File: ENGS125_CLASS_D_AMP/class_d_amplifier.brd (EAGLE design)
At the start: 100 x 80 mm, 24 parts, among them J1 BANANA_JACK_CT3151, J2 BANANA_JACK_CT3151, J3 BANANA_JACK_CT3151, J4 BANANA_JACK_CT3151, J5 BANANA_JACK_CT3151, J6 BANANA_JACK_CT3151, M1 BSC050NE2LSATMA1, M2 BSC050NE2LSATMA1, U1 LTC6992TSOT-23, U2 LTC4449

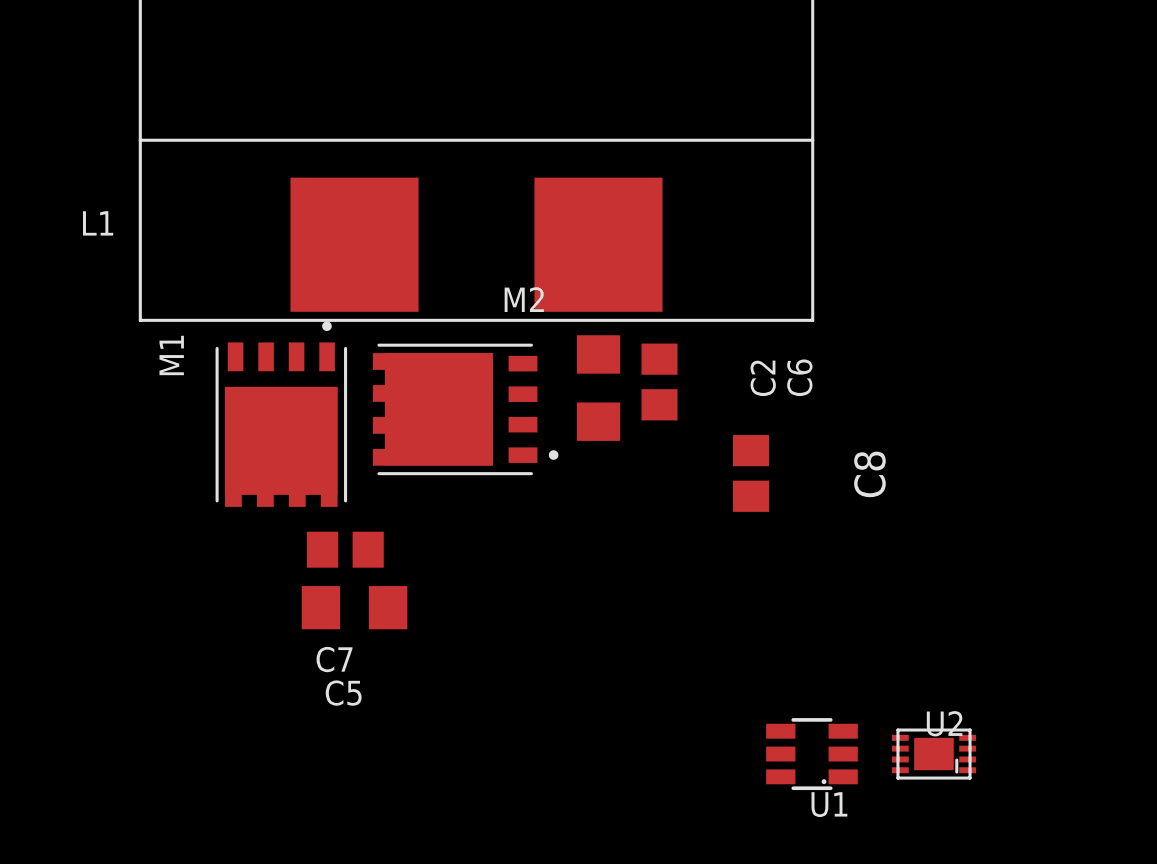
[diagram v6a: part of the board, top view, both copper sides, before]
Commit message: Generatedtop layer power polygons and placed vias
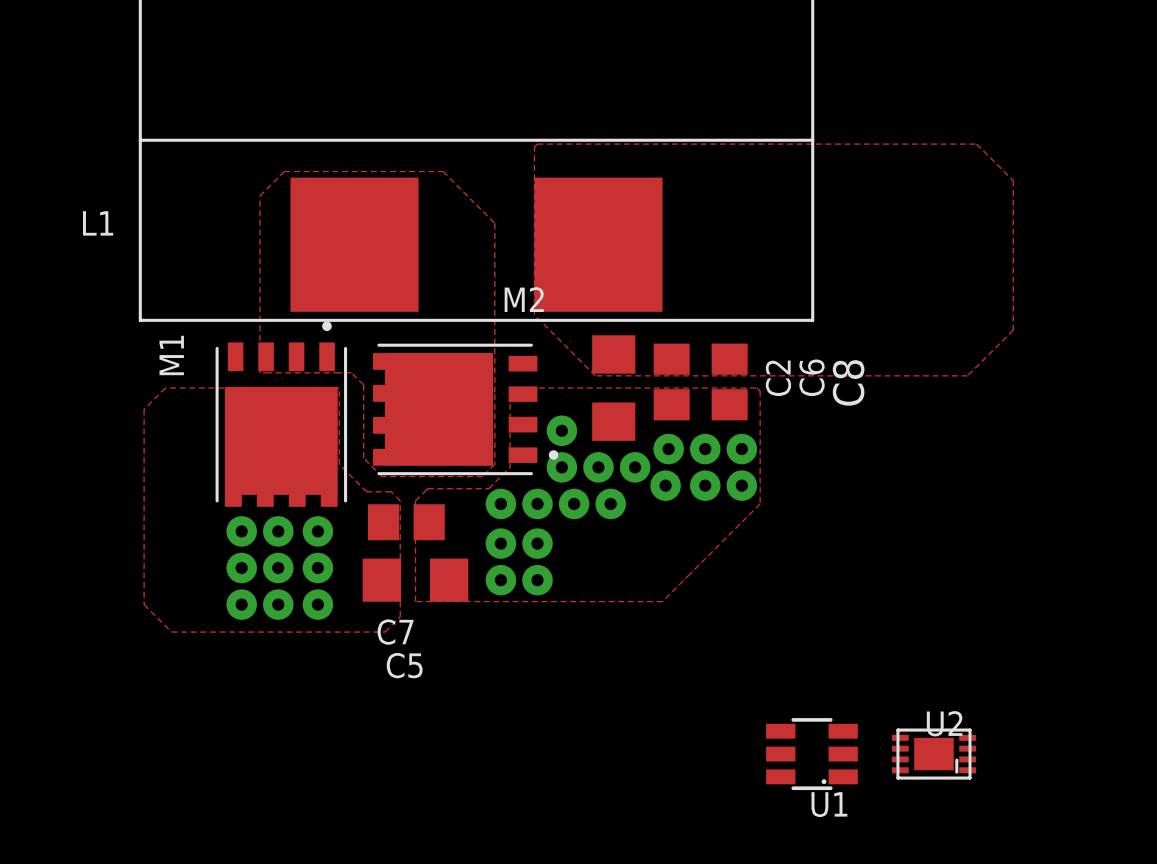
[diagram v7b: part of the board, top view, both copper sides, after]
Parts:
- moved C8 3.91 mm to (58.8, 30.7)
- moved C5 2.79 mm to (45.7, 22.5)
- moved C7 2.79 mm to (45.3, 24.9)
- moved C2 0.63 mm to (54.0, 30.5)
- moved C6 0.51 mm to (56.4, 30.7)
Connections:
- net VIN: now also M1.6, M1.7
- net VSW: now also M2.6, M2.7
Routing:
- added copper zone on layer 1, net GND
- added copper zone on layer 1, net VIN
- added copper zone on layer 1, net VOUT
- added copper zone on layer 1, net VSW

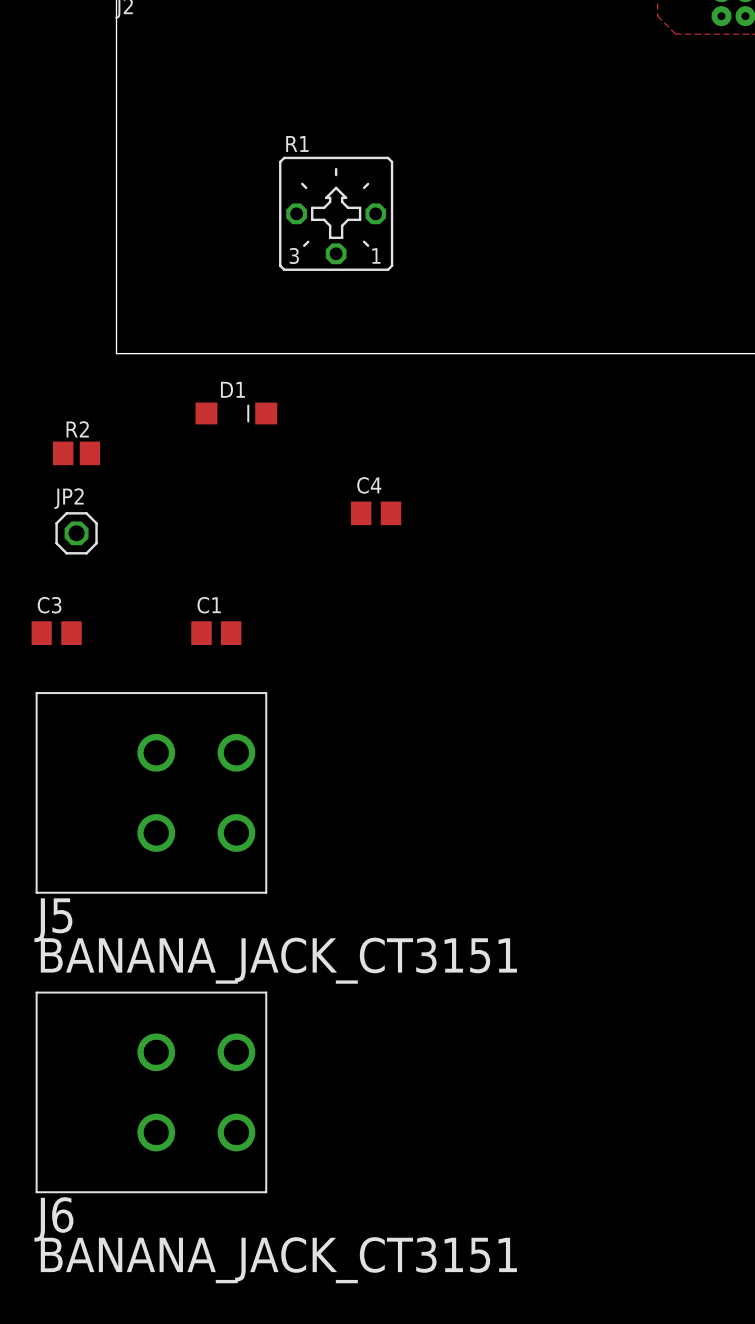
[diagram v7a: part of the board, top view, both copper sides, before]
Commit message: Removed component values from silkscreen
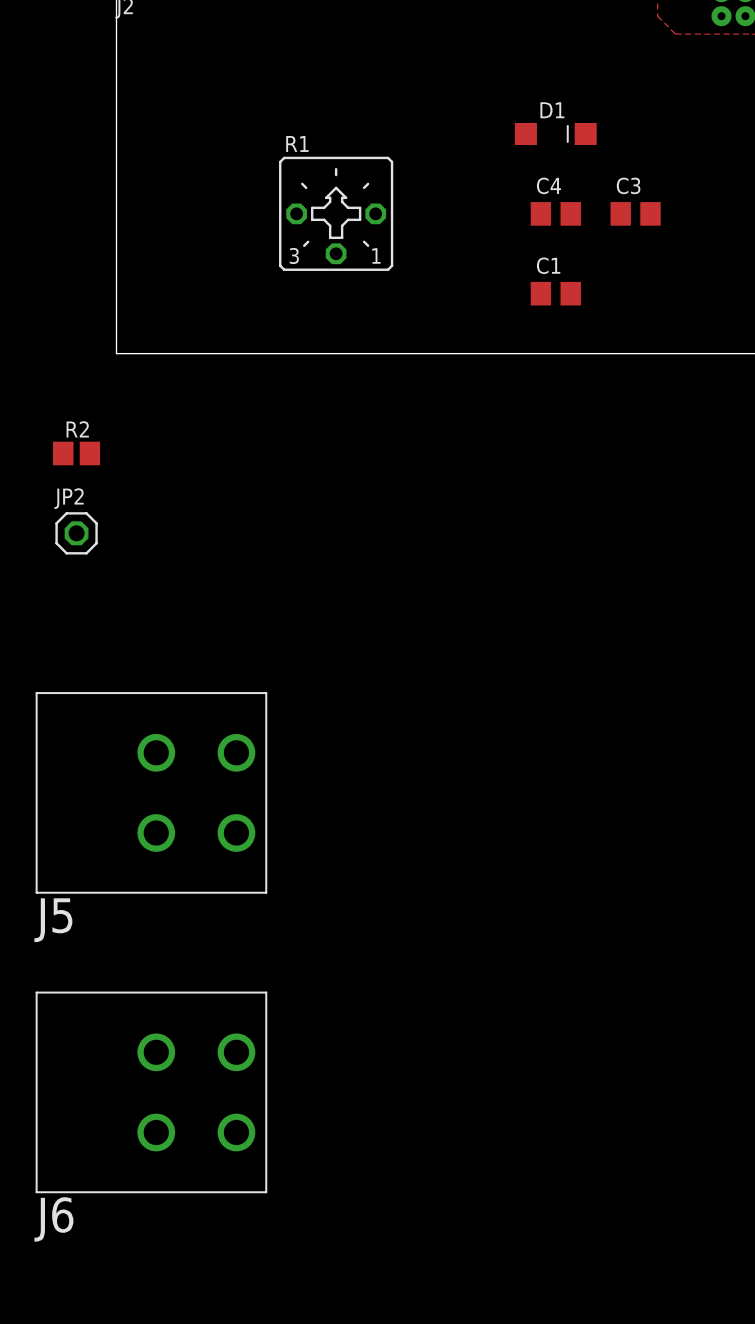
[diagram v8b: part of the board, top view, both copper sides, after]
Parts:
- moved C3 45.5 mm to (33.0, 8.89)
- moved C1 30.5 mm to (27.9, 3.81)
- moved D1 27.0 mm to (27.9, 14.0)
- moved C4 22.2 mm to (27.9, 8.89)
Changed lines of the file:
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@@
 </autorouter>
 <elements>
-<element name="C1" library="Engs125_library" package="C0805" value="0.1uF" x="6.35" y="-17.78" smashed="yes">
-<attribute name="NAME" x="5.08" y="-16.51" size="1.016" layer="25" font="fixed"/>
-<attribute name="VALUE" x="5.08" y="-20.32" size="1.016" layer="27" font="fixed"/>
+<element name="C1" library="Engs125_library" package="C0805" value="0.1uF" x="27.94" y="3.81" smashed="yes">
+<attribute name="NAME" x="26.67" y="5.08" size="1.016" layer="25" font="fixed"/>
 </element>
 <element name="C2" library="rcl" library_urn="urn:adsk.eagle:library:334" package="C1206" package3d_urn="urn:adsk.eagle:package:23618/2" value="1.5u" x="53.975" y="30.48" smashed="yes" rot="R270">
@@
 <attribute name="SPICEPREFIX" value="C" x="22.225" y="-15.24" size="1.778" layer="27" rot="R270" display="off"/>
 </element>
-<element name="C3" library="Engs125_library" package="C0805" value="1uF" x="-3.81" y="-17.78" smashed="yes">
-<attribute name="NAME" x="-5.08" y="-16.51" size="1.016" layer="25" font="fixed"/>
-<attribute name="VALUE" x="-5.08" y="-20.32" size="1.016" layer="27" font="fixed"/>
-</element>
-<element name="C4" library="Engs125_library" package="C0805" value="1uF" x="16.51" y="-10.16" smashed="yes">
-<attribute name="NAME" x="15.24" y="-8.89" size="1.016" layer="25" font="fixed"/>
-<attribute name="VALUE" x="15.24" y="-12.7" size="1.016" layer="27" font="fixed"/>
+<element name="C3" library="Engs125_library" package="C0805" value="1uF" x="33.02" y="8.89" smashed="yes">
+<attribute name="NAME" x="31.75" y="10.16" size="1.016" layer="25" font="fixed"/>
+</element>
+<element name="C4" library="Engs125_library" package="C0805" value="1uF" x="27.94" y="8.89" smashed="yes">
+<attribute name="NAME" x="26.67" y="10.16" size="1.016" layer="25" font="fixed"/>
 </element>
 <element name="C5" library="rcl" library_urn="urn:adsk.eagle:library:334" package="C1206" package3d_urn="urn:adsk.eagle:package:23618/2" value="4.7uF" x="45.72" y="22.479" smashed="yes">
@@
 <attribute name="NAME" x="44.069" y="19.812" size="1.016" layer="25" font="fixed"/>
 </element>
-<element name="D1" library="Engs125_library" package="SOD123" value="1N5819" x="7.62" y="-3.81" smashed="yes">
-<attribute name="NAME" x="6.52" y="-2.81" size="1.016" layer="25" font="fixed"/>
-<attribute name="VALUE" x="6.52" y="-6.11" size="1.016" layer="27" font="fixed"/>
+<element name="D1" library="Engs125_library" package="SOD123" value="1N5819" x="27.94" y="13.97" smashed="yes">
+<attribute name="NAME" x="26.84" y="14.97" size="1.016" layer="25" font="fixed"/>
 </element>
 <element name="L1" library="Engs125_library" package="SER2900" value="33u" x="48.26" y="50.8" smashed="yes">
@@
 <element name="J5" library="Engs125_lib_UPDATEFeb22" package="CT3151SP2_PCB_MOUNT" value="BANANA_JACK_CT3151" x="5.08" y="-27.94" smashed="yes">
 <attribute name="NAME" x="-5.08" y="-36.83" size="2.1844" layer="25" font="vector"/>
-<attribute name="VALUE" x="-5.08" y="-39.37" size="2.1844" layer="25" font="vector"/>
 </element>
 <element name="J6" library="Engs125_lib_UPDATEFeb22" package="CT3151SP2_PCB_MOUNT" value="BANANA_JACK_CT3151" x="5.08" y="-46.99" smashed="yes">
 <attribute name="NAME" x="-5.08" y="-55.88" size="2.1844" layer="25" font="vector"/>
-<attribute name="VALUE" x="-5.08" y="-58.42" size="2.1844" layer="25" font="vector"/>
 </element>
 <element name="C8" library="Engs125_library" package="C0805" value="0.1u" x="58.801" y="30.734" smashed="yes" rot="R270">
@@
 <wire x1="49.53" y1="5.08" x2="60.93" y2="16.19" width="0" layer="19" extent="1-1"/>
 <wire x1="46.99" y1="5.08" x2="49.53" y2="5.08" width="0" layer="19" extent="1-1"/>
-<wire x1="17.46" y1="-10.16" x2="46.99" y2="5.08" width="0" layer="19" extent="1-1"/>
-<wire x1="11.4554" y1="8.89" x2="17.46" y2="-10.16" width="0" layer="19" extent="1-1"/>
+<wire x1="28.89" y1="8.89" x2="46.99" y2="5.08" width="0" layer="19" extent="1-1"/>
+<wire x1="11.4554" y1="8.89" x2="28.89" y2="8.89" width="0" layer="19" extent="1-1"/>
 <wire x1="12.71" y1="27.93" x2="11.4554" y2="8.89" width="0" layer="19" extent="1-1"/>
 <wire x1="12.71" y1="33.03" x2="12.71" y2="27.93" width="0" layer="19" extent="1-1"/>
 <wire x1="7.61" y1="33.03" x2="12.71" y2="33.03" width="0" layer="19" extent="1-1"/>
 <wire x1="7.61" y1="27.93" x2="12.71" y2="27.93" width="0" layer="19" extent="1-1"/>
-<wire x1="-3.39" y1="-6.35" x2="17.46" y2="-10.16" width="0" layer="19" extent="1-1"/>
-<wire x1="-2.86" y1="-17.78" x2="-3.39" y2="-6.35" width="0" layer="19" extent="1-1"/>
-<wire x1="2.53" y1="-44.44" x2="-2.86" y2="-17.78" width="0" layer="19" extent="1-1"/>
+<wire x1="-3.39" y1="-6.35" x2="28.89" y2="8.89" width="0" layer="19" extent="1-1"/>
+<wire x1="33.97" y1="8.89" x2="-3.39" y2="-6.35" width="0" layer="19" extent="1-1"/>
+<wire x1="2.53" y1="-44.44" x2="33.97" y2="8.89" width="0" layer="19" extent="1-1"/>
 <wire x1="2.53" y1="-49.54" x2="2.53" y2="-44.44" width="0" layer="19" extent="1-1"/>
 <wire x1="7.63" y1="-49.54" x2="2.53" y2="-49.54" width="0" layer="19" extent="1-1"/>
@@
 <wire x1="65.91" y1="15.015" x2="65.91" y2="15.465" width="0" layer="19" extent="1-1"/>
 <wire x1="60.93" y1="15.24" x2="65.91" y2="15.465" width="0" layer="19" extent="1-1"/>
-<wire x1="15.56" y1="-10.16" x2="60.93" y2="15.24" width="0" layer="19" extent="1-1"/>
-<wire x1="5.72" y1="-3.81" x2="15.56" y2="-10.16" width="0" layer="19" extent="1-1"/>
-<wire x1="-4.76" y1="-17.78" x2="5.72" y2="-3.81" width="0" layer="19" extent="1-1"/>
-<wire x1="7.61" y1="43.17" x2="5.72" y2="-3.81" width="0" layer="19" extent="1-1"/>
+<wire x1="26.99" y1="8.89" x2="60.93" y2="15.24" width="0" layer="19" extent="1-1"/>
+<wire x1="26.04" y1="13.97" x2="26.99" y2="8.89" width="0" layer="19" extent="1-1"/>
+<wire x1="32.07" y1="8.89" x2="26.04" y2="13.97" width="0" layer="19" extent="1-1"/>
+<wire x1="7.61" y1="43.17" x2="26.04" y2="13.97" width="0" layer="19" extent="1-1"/>
 <wire x1="7.61" y1="48.27" x2="7.61" y2="43.17" width="0" layer="19" extent="1-1"/>
 <wire x1="12.71" y1="48.27" x2="7.61" y2="48.27" width="0" layer="19" extent="1-1"/>
@@
 <contactref element="U2" pad="8"/>
 <contactref element="C1" pad="1"/>
-<wire x1="9.52" y1="-3.81" x2="65.91" y2="14.565" width="0" layer="19" extent="1-1"/>
-<wire x1="5.4" y1="-17.78" x2="9.52" y2="-3.81" width="0" layer="19" extent="1-1"/>
+<wire x1="29.84" y1="13.97" x2="65.91" y2="14.565" width="0" layer="19" extent="1-1"/>
+<wire x1="26.99" y1="3.81" x2="29.84" y2="13.97" width="0" layer="19" extent="1-1"/>
 </signal>
 <signal name="VSW">
@@
 </polygon>
 <wire x1="46.696" y1="29.591" x2="68.71" y2="15.015" width="0" layer="19" extent="1-1"/>
-<wire x1="7.3" y1="-17.78" x2="44.196" y2="27.596" width="0" layer="19" extent="1-1"/>
+<wire x1="28.89" y1="3.81" x2="44.196" y2="27.596" width="0" layer="19" extent="1-1"/>
 </signal>
 <signal name="VOUT">
